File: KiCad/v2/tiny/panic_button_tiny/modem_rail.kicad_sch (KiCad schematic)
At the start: 1 part, among them U4 TPS61022

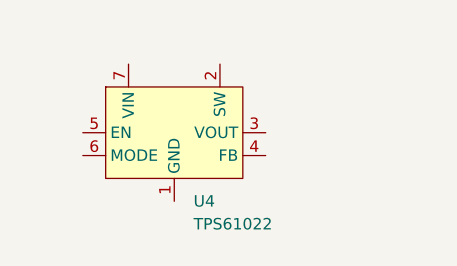
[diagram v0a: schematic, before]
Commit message: [UPDATE] the schematic with a buzzer and wirering for the different components
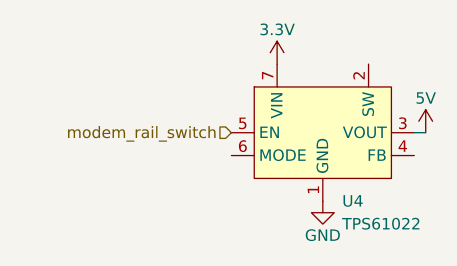
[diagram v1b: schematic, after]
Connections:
- net GND: now reaches U4.1 (GND)
- net 5V: now reaches U4.3 (VOUT)
- net modem_rail_switch: now reaches U4.5 (EN)
- net 3.3V: now reaches U4.7 (VIN)
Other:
- moved on the sheet: U4
